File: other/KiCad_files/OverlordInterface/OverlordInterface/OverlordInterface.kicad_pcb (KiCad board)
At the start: 2 copper layers, 155 x 42 mm, 12 parts, among them J1 Conn_01x12_Female, J2 DE9_Receptacle_MountingHoles_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, J3 DE9_Receptacle_MountingHoles_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, J4 DE9_Receptacle_MountingHoles_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, J5 DE9_Receptacle_MountingHoles_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

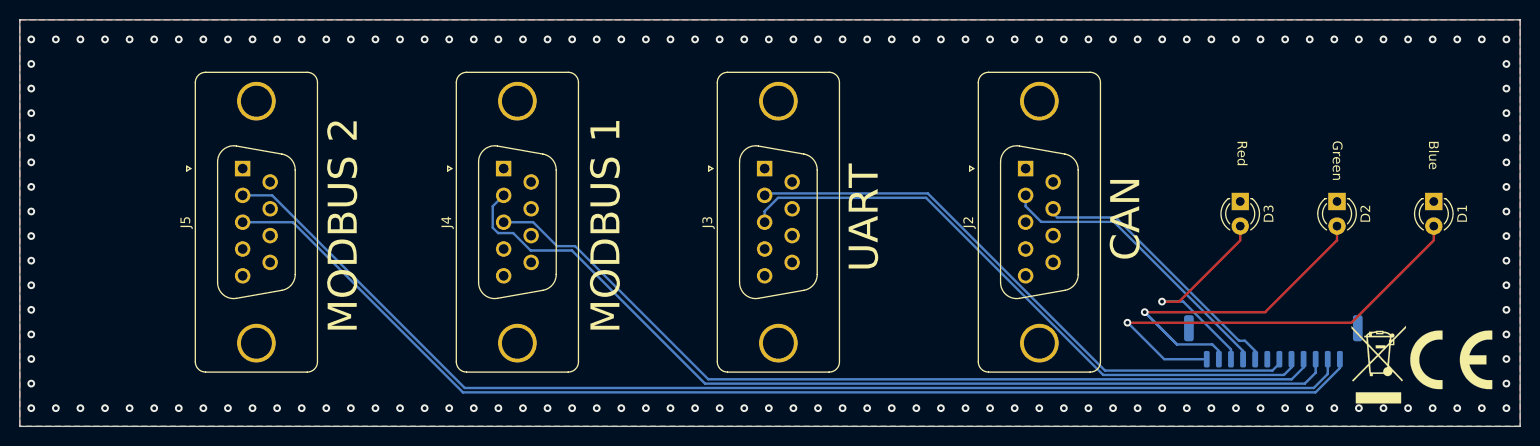
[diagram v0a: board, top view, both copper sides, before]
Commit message: sent to production
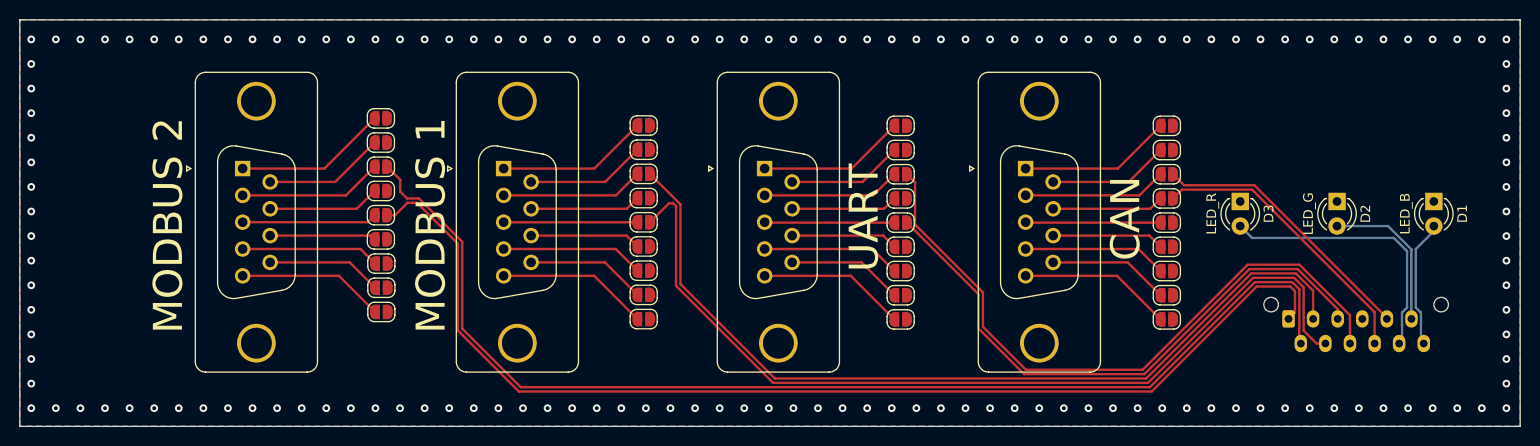
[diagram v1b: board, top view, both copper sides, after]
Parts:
- removed REF** (x2): CE-Logo_8.5x6mm_SilkScreen, Symbol:CE-Logo_8.5x6mm_SilkScreen
- removed REF** (x2): WEEE-Logo_5.6x8mm_SilkScreen, Symbol:WEEE-Logo_5.6x8mm_SilkScreen
- added JP1: SolderJumper_2_Open, Jumper:SolderJumper-2_P1.3mm_Open_RoundedPad1.0x1.5mm, F.Cu at (166.7, 83.2)
- added JP10: SolderJumper_2_Open, Jumper:SolderJumper-2_P1.3mm_Open_RoundedPad1.0x1.5mm, F.Cu at (194.2, 85.7)
- added JP11: SolderJumper_2_Open, Jumper:SolderJumper-2_P1.3mm_Open_RoundedPad1.0x1.5mm, F.Cu at (194.2, 88.2)
- added JP12: SolderJumper_2_Open, Jumper:SolderJumper-2_P1.3mm_Open_RoundedPad1.0x1.5mm, F.Cu at (194.2, 90.7)
- added JP13: SolderJumper_2_Open, Jumper:SolderJumper-2_P1.3mm_Open_RoundedPad1.0x1.5mm, F.Cu at (194.2, 93.2)
- added JP14: SolderJumper_2_Open, Jumper:SolderJumper-2_P1.3mm_Open_RoundedPad1.0x1.5mm, F.Cu at (194.2, 95.7)
- added JP15: SolderJumper_2_Open, Jumper:SolderJumper-2_P1.3mm_Open_RoundedPad1.0x1.5mm, F.Cu at (194.2, 98.2)
- added JP16: SolderJumper_2_Open, Jumper:SolderJumper-2_P1.3mm_Open_RoundedPad1.0x1.5mm, F.Cu at (194.2, 100.7)
- added JP17: SolderJumper_2_Open, Jumper:SolderJumper-2_P1.3mm_Open_RoundedPad1.0x1.5mm, F.Cu at (194.2, 103.2)
- added JP18: SolderJumper_2_Open, Jumper:SolderJumper-2_P1.3mm_Open_RoundedPad1.0x1.5mm, F.Cu at (140.2, 83.2)
- added JP19: SolderJumper_2_Open, Jumper:SolderJumper-2_P1.3mm_Open_RoundedPad1.0x1.5mm, F.Cu at (140.2, 85.7)
- added JP2: SolderJumper_2_Open, Jumper:SolderJumper-2_P1.3mm_Open_RoundedPad1.0x1.5mm, F.Cu at (166.7, 85.7)
- added JP20: SolderJumper_2_Open, Jumper:SolderJumper-2_P1.3mm_Open_RoundedPad1.0x1.5mm, F.Cu at (140.2, 88.2)
- added JP21: SolderJumper_2_Open, Jumper:SolderJumper-2_P1.3mm_Open_RoundedPad1.0x1.5mm, F.Cu at (140.2, 90.7)
- added JP22: SolderJumper_2_Open, Jumper:SolderJumper-2_P1.3mm_Open_RoundedPad1.0x1.5mm, F.Cu at (140.2, 93.2)
- added JP23: SolderJumper_2_Open, Jumper:SolderJumper-2_P1.3mm_Open_RoundedPad1.0x1.5mm, F.Cu at (140.2, 95.7)
- added JP24: SolderJumper_2_Open, Jumper:SolderJumper-2_P1.3mm_Open_RoundedPad1.0x1.5mm, F.Cu at (140.2, 98.2)
- added JP25: SolderJumper_2_Open, Jumper:SolderJumper-2_P1.3mm_Open_RoundedPad1.0x1.5mm, F.Cu at (140.2, 100.7)
- added JP26: SolderJumper_2_Open, Jumper:SolderJumper-2_P1.3mm_Open_RoundedPad1.0x1.5mm, F.Cu at (140.2, 103.2)
- added JP27: SolderJumper_2_Open, Jumper:SolderJumper-2_P1.3mm_Open_RoundedPad1.0x1.5mm, F.Cu at (113.0, 82.5)
- added JP28: SolderJumper_2_Open, Jumper:SolderJumper-2_P1.3mm_Open_RoundedPad1.0x1.5mm, F.Cu at (113.0, 85.0)
- added JP29: SolderJumper_2_Open, Jumper:SolderJumper-2_P1.3mm_Open_RoundedPad1.0x1.5mm, F.Cu at (113.0, 87.5)
- added JP3: SolderJumper_2_Open, Jumper:SolderJumper-2_P1.3mm_Open_RoundedPad1.0x1.5mm, F.Cu at (166.7, 88.2)
- added JP30: SolderJumper_2_Open, Jumper:SolderJumper-2_P1.3mm_Open_RoundedPad1.0x1.5mm, F.Cu at (113.0, 90.0)
- added JP31: SolderJumper_2_Open, Jumper:SolderJumper-2_P1.3mm_Open_RoundedPad1.0x1.5mm, F.Cu at (113.0, 92.5)
- added JP32: SolderJumper_2_Open, Jumper:SolderJumper-2_P1.3mm_Open_RoundedPad1.0x1.5mm, F.Cu at (113.0, 95.0)
- added JP33: SolderJumper_2_Open, Jumper:SolderJumper-2_P1.3mm_Open_RoundedPad1.0x1.5mm, F.Cu at (113.1, 97.5)
- added JP34: SolderJumper_2_Open, Jumper:SolderJumper-2_P1.3mm_Open_RoundedPad1.0x1.5mm, F.Cu at (113.1, 100.0)
- added JP35: SolderJumper_2_Open, Jumper:SolderJumper-2_P1.3mm_Open_RoundedPad1.0x1.5mm, F.Cu at (113.1, 102.5)
- added JP36: SolderJumper_2_Open, Jumper:SolderJumper-2_P1.3mm_Open_RoundedPad1.0x1.5mm, F.Cu at (166.7, 103.2)
- added JP4: SolderJumper_2_Open, Jumper:SolderJumper-2_P1.3mm_Open_RoundedPad1.0x1.5mm, F.Cu at (166.7, 90.7)
- added JP5: SolderJumper_2_Open, Jumper:SolderJumper-2_P1.3mm_Open_RoundedPad1.0x1.5mm, F.Cu at (166.7, 93.2)
- added JP6: SolderJumper_2_Open, Jumper:SolderJumper-2_P1.3mm_Open_RoundedPad1.0x1.5mm, F.Cu at (166.7, 95.7)
- added JP7: SolderJumper_2_Open, Jumper:SolderJumper-2_P1.3mm_Open_RoundedPad1.0x1.5mm, F.Cu at (166.7, 98.2)
- added JP8: SolderJumper_2_Open, Jumper:SolderJumper-2_P1.3mm_Open_RoundedPad1.0x1.5mm, F.Cu at (166.7, 100.7)
- added JP9: SolderJumper_2_Open, Jumper:SolderJumper-2_P1.3mm_Open_RoundedPad1.0x1.5mm, F.Cu at (194.2, 83.2)
- J1: value Conn_01x12_Female -> Conn_01x12_Pin; footprint Connector_Molex:Molex_CLIK-Mate_502386-1270_1x12-1MP_P1.25mm_Horizontal -> Connector_Molex:Molex_Picoflex_90325-0012_2x06_P1.27mm_Vertical
- moved J1 2.79 mm to (206.8, 103.2), turned to -90 degrees
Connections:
- J1 pad 1: STATUS_LED_B -> MB_RX_U2
- J1 pad 10: MB_TX_U1 -> STATUS_LED_R
- J1 pad 11: MB_TX_U2 -> STATUS_LED_G
- J1 pad 12: MB_RX_U2 -> STATUS_LED_B
- J1 pad 2: STATUS_LED_G -> MB_TX_U2
- J1 pad 3: STATUS_LED_R -> MB_TX_U1
- J1 pad 4: CAN_L -> MB_RX_U1
- J1 pad 5: CAN_H -> RS232_RX
- J1 pad 6: GND -> RS232_TX
- J1 pad 7: UART_TX_0 -> GND
- J1 pad 8: UART_RX_0 -> CAN_H
- J1 pad 9: MB_RX_U1 -> CAN_L
- J2 pad 1: unconnected-(J2-Pad1) -> Net-(JP9-B)
- J2 pad 2: CAN_L -> Net-(JP11-B)
- J2 pad 3: GND -> Net-(JP13-B)
- J2 pad 4: unconnected-(J2-Pad4) -> Net-(JP15-B)
- J2 pad 5: unconnected-(J2-Pad5) -> Net-(JP17-B)
- J2 pad 6: unconnected-(J2-Pad6) -> Net-(JP10-B)
- J2 pad 7: CAN_H -> Net-(JP12-B)
- J2 pad 8: unconnected-(J2-Pad8) -> Net-(JP14-B)
- J2 pad 9: unconnected-(J2-Pad9) -> Net-(JP16-B)
- J3 pad 1: unconnected-(J3-Pad1) -> Net-(JP1-B)
- J3 pad 2: UART_TX_0 -> Net-(JP3-B)
- J3 pad 3: UART_RX_0 -> Net-(JP5-B)
- J3 pad 4: unconnected-(J3-Pad4) -> Net-(JP7-B)
- J3 pad 5: GND -> Net-(JP36-B)
- J3 pad 6: unconnected-(J3-Pad6) -> Net-(JP2-B)
- J3 pad 7: unconnected-(J3-Pad7) -> Net-(JP4-B)
- J3 pad 8: unconnected-(J3-Pad8) -> Net-(JP6-B)
- J3 pad 9: unconnected-(J3-Pad9) -> Net-(JP8-B)
- J4 pad 1: unconnected-(J4-Pad1) -> Net-(JP18-B)
- J4 pad 2: MB_TX_U1 -> Net-(JP20-B)
- J4 pad 3: MB_RX_U1 -> Net-(JP22-B)
- J4 pad 4: unconnected-(J4-Pad4) -> Net-(JP24-B)
- J4 pad 5: GND -> Net-(JP26-B)
- J4 pad 6: unconnected-(J4-Pad6) -> Net-(JP19-B)
- J4 pad 7: unconnected-(J4-Pad7) -> Net-(JP21-B)
- J4 pad 8: unconnected-(J4-Pad8) -> Net-(JP23-B)
- J4 pad 9: unconnected-(J4-Pad9) -> Net-(JP25-B)
- J5 pad 1: unconnected-(J5-Pad1) -> Net-(JP27-B)
- J5 pad 2: MB_TX_U2 -> Net-(JP29-B)
- J5 pad 3: MB_RX_U2 -> Net-(JP31-B)
- J5 pad 4: unconnected-(J5-Pad4) -> Net-(JP33-B)
- J5 pad 5: GND -> Net-(JP35-B)
- J5 pad 6: unconnected-(J5-Pad6) -> Net-(JP28-B)
- J5 pad 7: unconnected-(J5-Pad7) -> Net-(JP30-B)
- J5 pad 8: unconnected-(J5-Pad8) -> Net-(JP32-B)
- J5 pad 9: unconnected-(J5-Pad9) -> Net-(JP34-B)
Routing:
- net RS232_TX: track 0.00 -> 68.3 mm
- net UART_RX_0: track 64.9 -> 0.00 mm
- net UART_TX_0: track 61.6 -> 0.00 mm
- net RS232_RX: track 0.00 -> 60.3 mm
- net STATUS_LED_B: track 46.5 -> 13.2 mm, vias 1 -> 0
- net STATUS_LED_G: track 39.0 -> 15.9 mm, vias 1 -> 0
- net Net-(JP17-B): track 0.00 -> 15.8 mm
- net Net-(JP27-B): track 0.00 -> 15.8 mm
- net Net-(JP9-B): track 0.00 -> 15.8 mm
- net Net-(JP26-B): track 0.00 -> 15.7 mm
- net Net-(JP18-B): track 0.00 -> 15.7 mm
- net Net-(JP36-B): track 0.00 -> 15.3 mm
- net Net-(JP1-B): track 0.00 -> 15.2 mm
- net Net-(JP35-B): track 0.00 -> 15.2 mm
- net Net-(JP15-B): track 0.00 -> 14.9 mm
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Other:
- board text added: "--- Overlord Interface --- Designed by Nimfrodian Ver 1.0 Rev B"
- board text removed: "--- Overlord Interface --- Designed by Nimfrodian Ver 1.0 Rev A"
- board text removed: "Blue"
- board text removed: "Green"
- board text removed: "Red"

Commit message: sent to production with fixes
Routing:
- net RS232_RX: track 60.3 -> 62.6 mm
- net MB_RX_U2: track 115.5 -> 117.3 mm
- net MB_TX_U2: track 120.1 -> 121.9 mm
- net RS232_TX: track 68.3 -> 69.8 mm
- net MB_RX_U1: track 93.0 -> 94.4 mm
- net MB_TX_U1: track 90.2 -> 91.6 mm
- net GND: vias 150 -> 151
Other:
- board text added: "--- Overlord Interface --- Designed by Nimfrodian Ver 1.0 Rev C"
- board text added: "RS232"
- board text removed: "--- Overlord Interface --- Designed by Nimfrodian Ver 1.0 Rev B"
- board text removed: "UART"
